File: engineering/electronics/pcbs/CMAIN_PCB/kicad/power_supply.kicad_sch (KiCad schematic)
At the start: 63 parts, among them J25 ${ALTIUM_VALUE}, J26 ${ALTIUM_VALUE}, J28 ${ALTIUM_VALUE}, J34 ${ALTIUM_VALUE}, J42 ${ALTIUM_VALUE}, J44 ${ALTIUM_VALUE}, Q4 PSMN4R3-30BL,118, Q5 PSMN4R3-30BL,118, Q6 ${ALTIUM_VALUE}, Q7 ${ALTIUM_VALUE}, Q8 PSMN4R3-30BL,118, Q9 ${ALTIUM_VALUE}, U29 LTC4370IMS#PBF, U30 LTC4370IMS#PBF, U31 LTC4370IMS#PBF

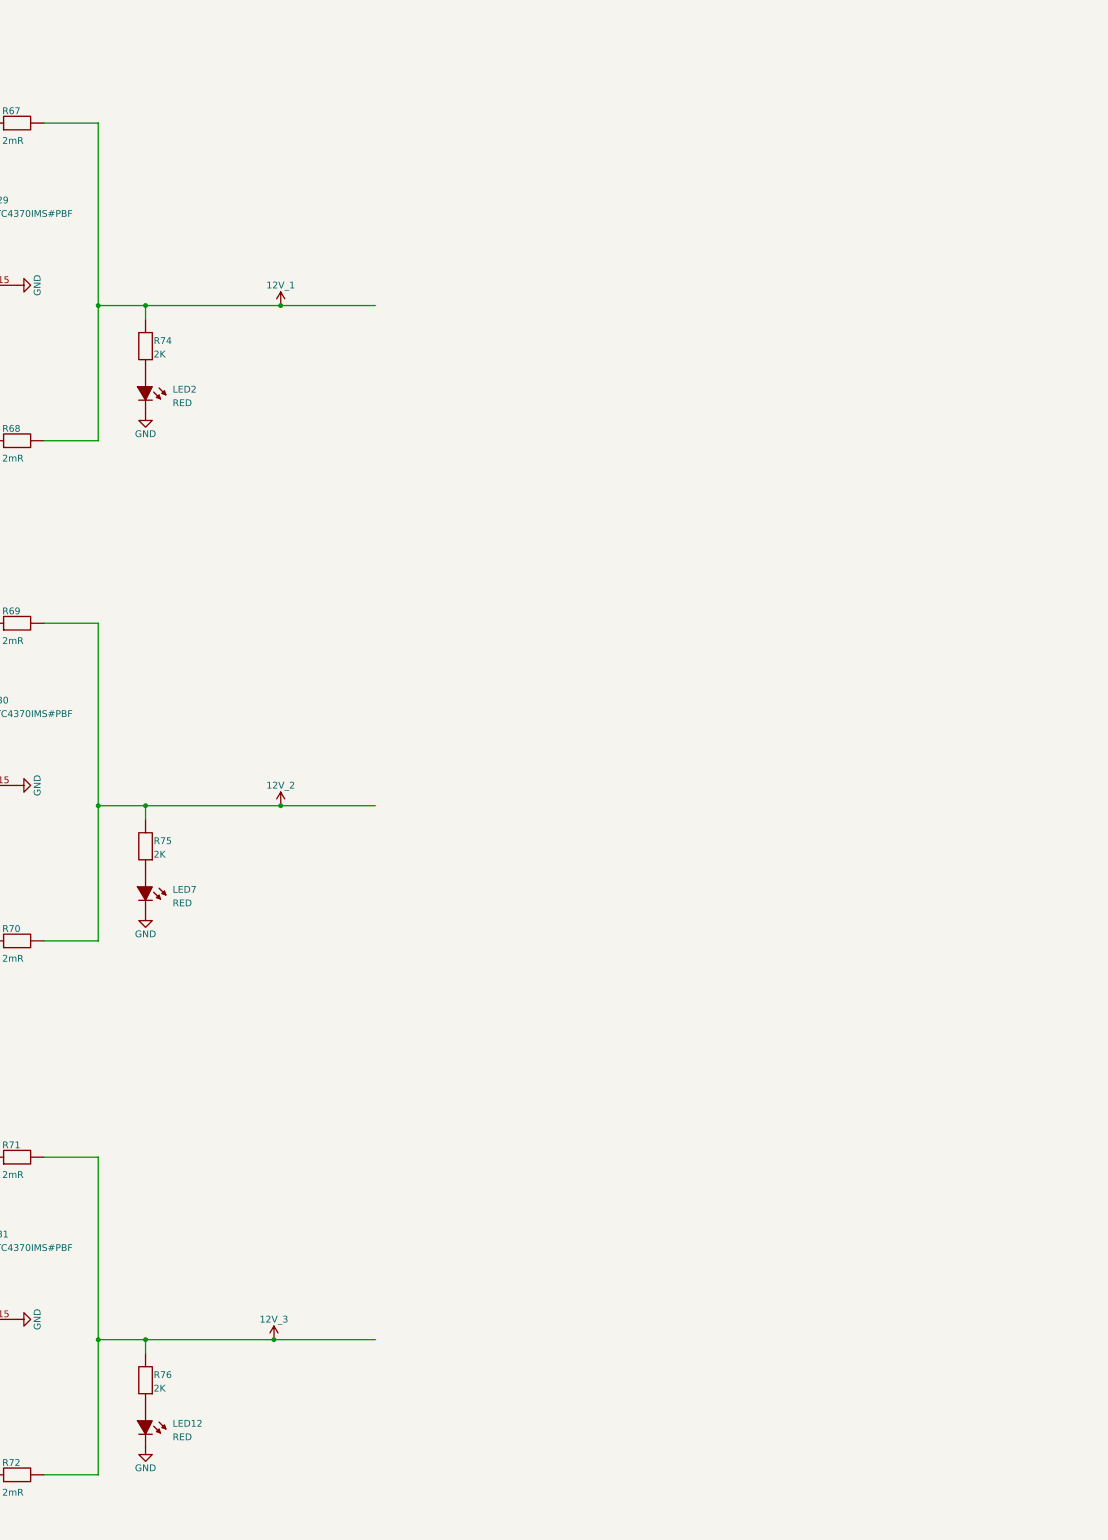
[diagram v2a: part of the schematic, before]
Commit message: electronics: integrate June PCB updates
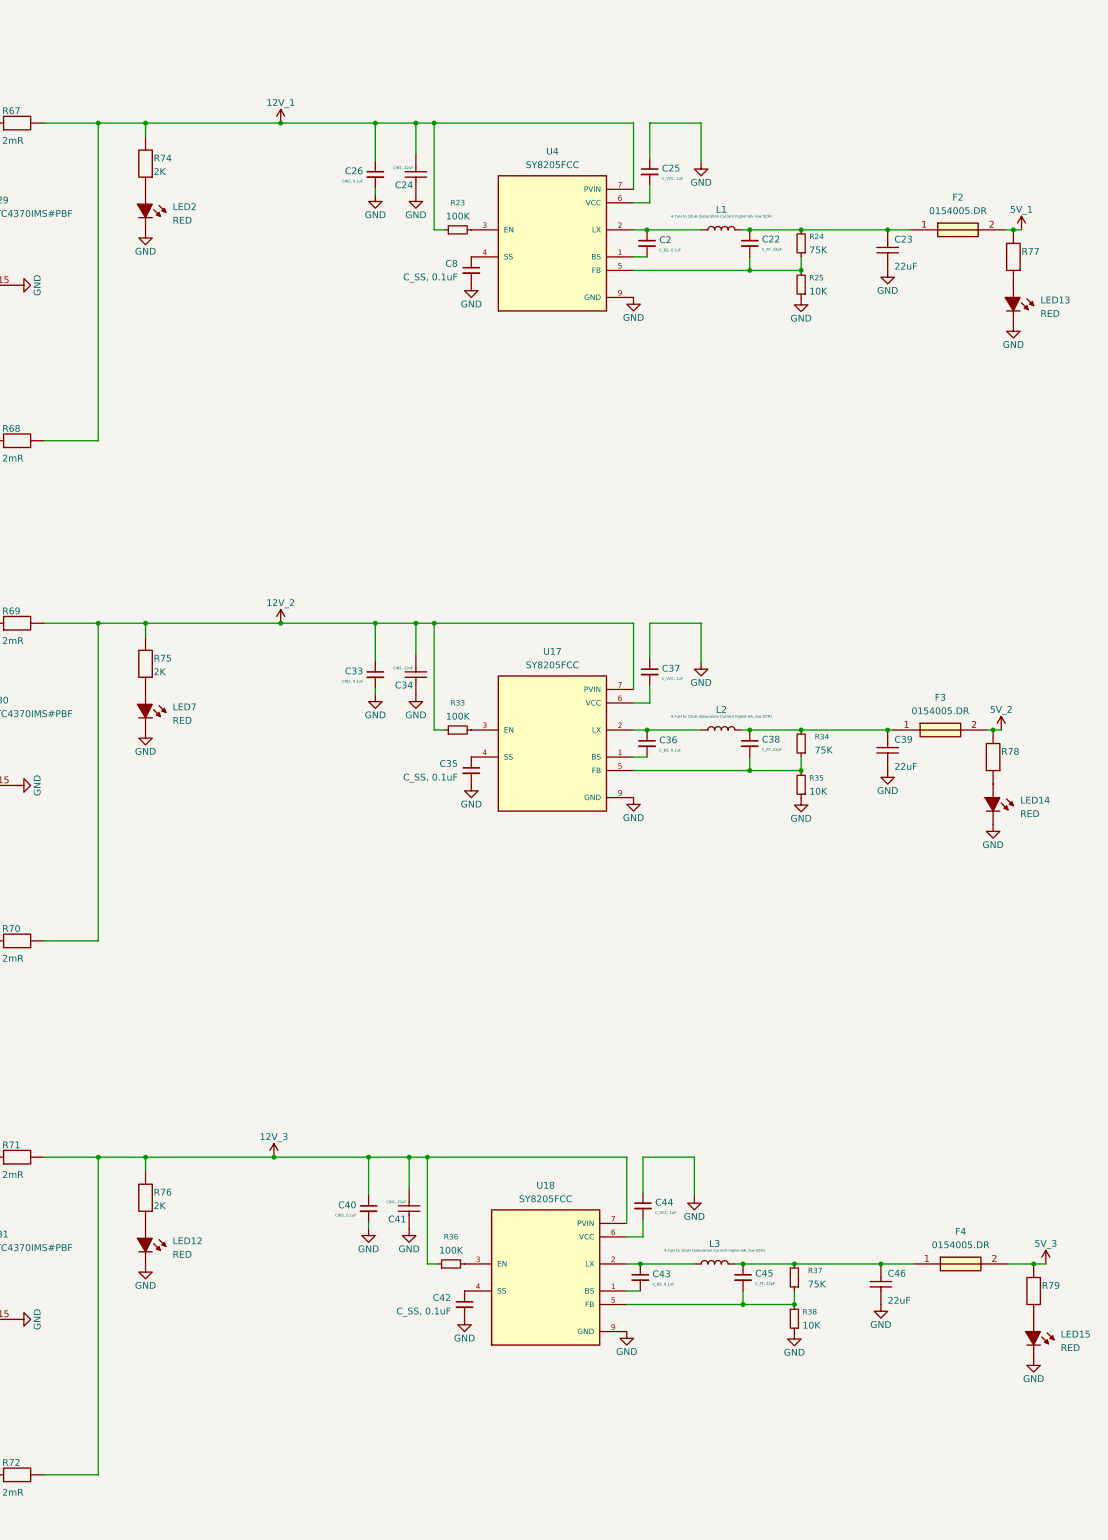
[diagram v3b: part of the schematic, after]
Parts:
- added C2, C36, C43: C_BS, 0.1uF, symbol Device:C_Small
- added C22, C38, C45: C_FF, 22pF, symbol Device:C_Small
- added C23, C39, C46: 22uF, C1206, symbol Signal Distribution Box-altium-import:root_1_10uF ± 10% 25V
- added C24, C34, C41: CIN1, 22uF, C1206, symbol Signal Distribution Box-altium-import:root_1_10uF ± 10% 25V
- added C25, C37, C44: C_VCC, 1uF, symbol Device:C_Small
- added C26, C33, C40: CIN2, 0.1uF, symbol Device:C_Small
- added C35, C42, C8: C_SS, 0.1uF, symbol Device:C_Small
- added F2, F3, F4: 0154005.DR, Samacsys:0154005DR, symbol Samacsys_kicad_sym:0154005.DR
- added L1, L2, L3: 4.7uH to 10uH (Saturation Current higher 6A, low 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, symbol Device:L
- added LED13, LED14, LED15: ${ALTIUM_VALUE}, LED_PLCC2, symbol Signal Distribution Box-altium-import:root_3_LED_SMD
- added R23, R33, R36: 100K, symbol Device:R_Small
- added R24, R34, R37: 75K, symbol Device:R_Small
- added R25, R35, R38: 10K, symbol Device:R_Small
- added R77, R78, R79: (no value), R0805, symbol Signal Distribution Box-altium-import:root_1_2 kOhms ±1% 0.125W
- added U17, U18, U4: SY8205FCC, SY8205FCC:VREG_SY8205FCC, symbol CMAIN_PCB:SY8205FCC
- J25, J26, J28, J34, J42, J44: symbol CBC_PCB:AT13-08PA-BM01 -> CMAIN_PCB:AT13-08PA-BM01
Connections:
- net 12V_2 is gone; now on net 12V_1: R69.2, R70.2, R75.2
- net 12V_3 is gone; now on net 12V_1: R71.2, R72.2, R76.2
- net 12V_1: now also C24.1, C26.1, C33.1, C34.1, C40.1, C41.1, R23.1, R33.1, R36.1, U17.7 (PVIN), U17.8 (PVIN), U18.7 (PVIN), U18.8 (PVIN), U4.7 (PVIN), U4.8 (PVIN)
- net GND: now also C23.1, C24.2, C25.1, C26.2, C33.2, C34.2, C35.2, C37.1, C39.1, C40.2, C41.2, C42.2, C44.1, C46.1, C8.2, LED13.C, LED14.C, LED15.C, R25.1, R35.1, R38.1, U17.9 (GND), U18.9 (GND), U4.9 (GND)
- new net: C38.2, R34.1, R35.2, U17.5 (FB)
- new net: C44.2, U18.6 (VCC)
- new net: C35.1, U17.4 (SS)
- new net: C2.1, L1.1, U4.2 (LX)
- new net: C22.1, C23.2, F2.1, L1.2, R24.2
- new net: C36.1, L2.1, U17.2 (LX)
- new net: C38.1, C39.2, F3.1, L2.2, R34.2
- new net: R23.2, U4.3 (EN)
- new net: LED14.A, R78.1
- new net: C45.1, C46.2, F4.1, L3.2, R37.2
- new net: C8.1, U4.4 (SS)
- new net: LED15.A, R79.1
- new net: LED13.A, R77.1
- new net: C45.2, R37.1, R38.2, U18.5 (FB)
- new net: R33.2, U17.3 (EN)
- new net: C43.2, U18.1 (BS)
- new net: C43.1, L3.1, U18.2 (LX)
- new net: R36.2, U18.3 (EN)
- new net: C42.1, U18.4 (SS)
- new net: C22.2, R24.1, R25.2, U4.5 (FB)
- new net: C2.2, U4.1 (BS)
- new net: C37.2, U17.6 (VCC)
- new net: C25.2, U4.6 (VCC)
- new net: C36.2, U17.1 (BS)
- new net 5V_1: F2.2, R77.2
- new net 5V_2: F3.2, R78.2
- new net 5V_3: F4.2, R79.2
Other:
- moved on the sheet: LED12, LED2, LED7, R74, R75, R76

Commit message: electronics: clean up CMAIN local libraries
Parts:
- C10, C11, C12, C15, C16, C23, C24, C34, C39, C41, C46, C9: footprint C1206 -> EasyEDA_Lib:C1206
- C13, C14, C17, C18, C20, C21: footprint CAP_EEUFC1E101S -> EasyEDA_Lib:CAP-TH_BD10.0-P5.00-D0.6-FD_2
- C27, C28, C29, C30, C31, C32: footprint C0805 -> CMAIN_PCB:C_0805_2012Metric_Pad1.18x1.45mm_HandSolder
- D12, D13, D14, D15, D16, D17: footprint DO-214AA2 -> CMAIN_PCB:D_SMB
- J25, J26, J28, J34, J42, J44: footprint CBC_PCB:AT13-08PA-BM01 -> CMAIN_PCB:AT13-08PA-BM01
- LED1, LED10, LED11, LED12, LED13, LED14, LED15, LED2, LED3, LED7, LED8, LED9: footprint LED_PLCC2 -> CMAIN_PCB:LEDC2012X85N
- Q4, Q5, Q6, Q7, Q8, Q9: footprint TRANS_PSMN4R8-100BSE -> CMAIN_PCB:POWERPAK-SO-8_L5.9-W4.9-P1.27-LS6.2-BL
- R33: footprint (none) -> CMAIN_PCB:R_0805_2012Metric_Pad1.20x1.40mm_HandSolder
- R50, R51, R52, R53, R54, R55, R74, R75, R76, R77, R78, R79: footprint R0805 -> CMAIN_PCB:R_0805_2012Metric_Pad1.20x1.40mm_HandSolder
- R67, R68, R69, R70, R71, R72: footprint R2512 -> CMAIN_PCB:R_2512_6332Metric
- U17, U18, U4: footprint SY8205FCC:VREG_SY8205FCC -> CMAIN_PCB:VREG_SY8205FCC
- U29, U30, U31: footprint SOP50P490X110-16N -> CMAIN_PCB:MSOP-16_3x4.039mm_P0.5mm
